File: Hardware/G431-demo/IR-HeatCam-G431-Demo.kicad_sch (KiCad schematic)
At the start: 5 parts, among them J1 Conn_SDCard, J3 Conn_UART, J4 Conn_I2C, J5 Conn_ADC1, J6 Conn_ADC2

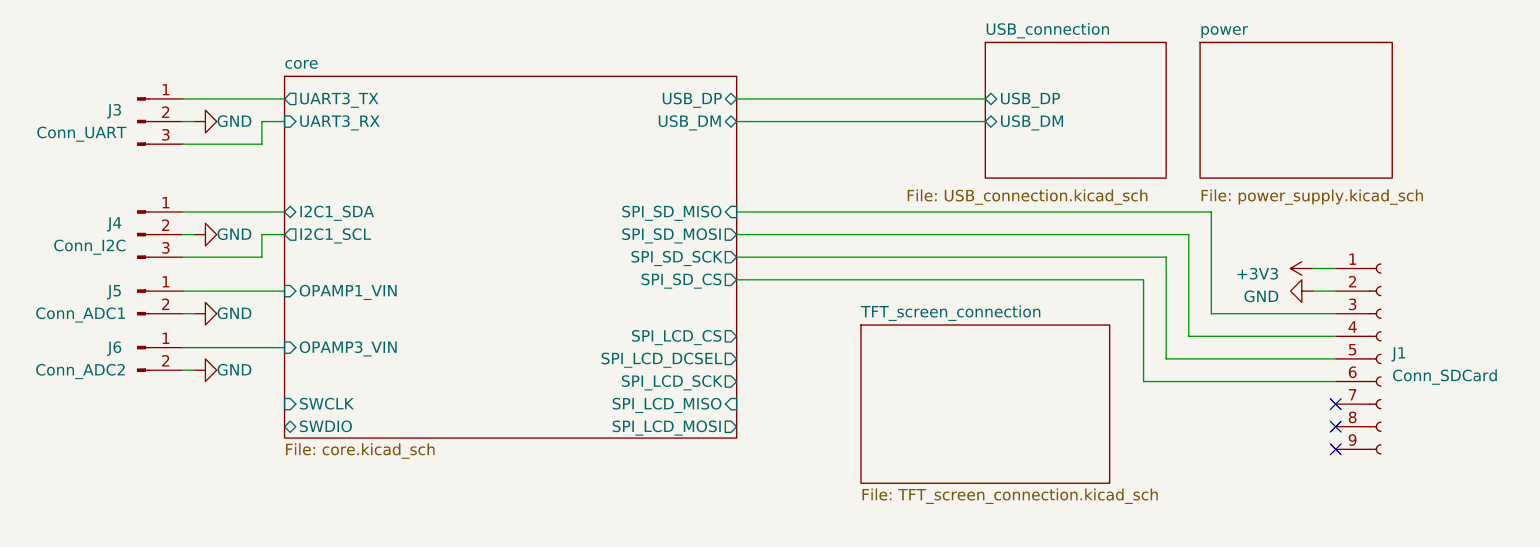
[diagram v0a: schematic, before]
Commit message: Schemetic done; PCB component layout
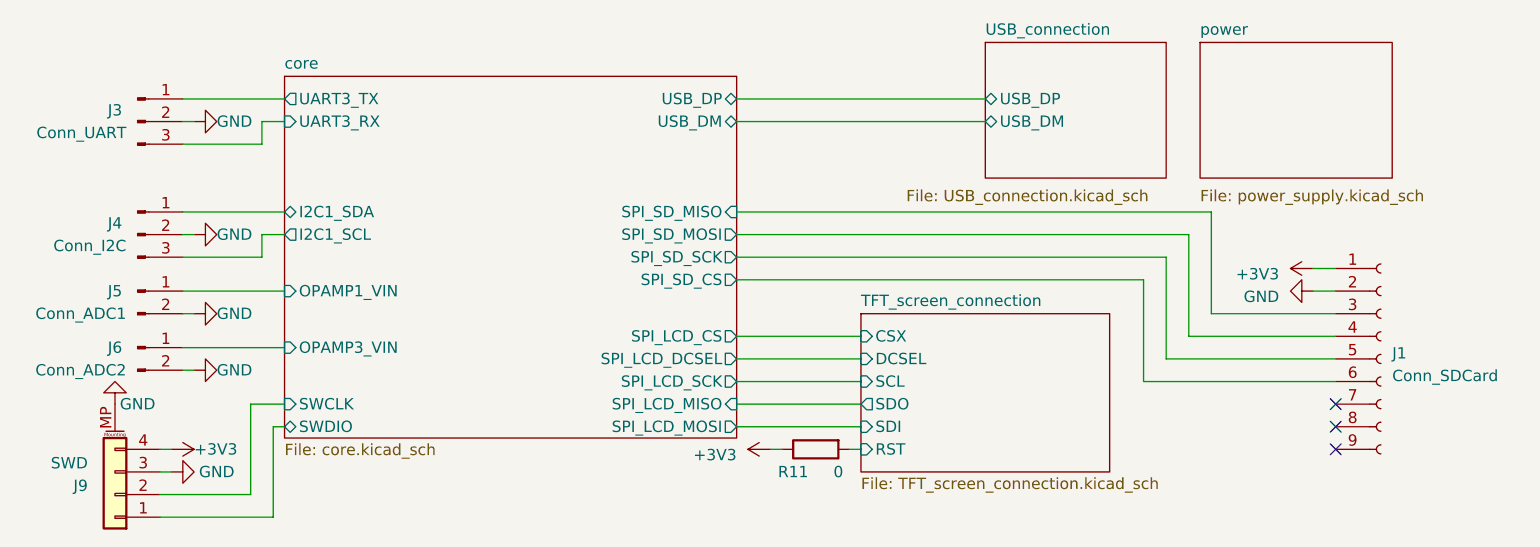
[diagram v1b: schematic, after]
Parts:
- added J9: SWD, Connector_Molex:Molex_PicoBlade_53261-0471_1x04-1MP_P1.25mm_Horizontal, symbol Connector_Generic_MountingPin:Conn_01x04_MountingPin
- added R11: 0, Resistor_SMD:R_0603_1608Metric, symbol Device:R
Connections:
- net +3V3: now also J9.4 (Pin_4), R11.1
- net GND: now also J9.3 (Pin_3), J9.MP (MountPin)
- net core/SWCLK: now also J9.2 (Pin_2)
- net core/SWDIO: now also J9.1 (Pin_1)
- new net TFT_screen_connection/RST: R11.2
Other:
- sheet TFT_screen_connection ports: added CSX, DCSEL, RST, SCL, SDI, SDO; removed none
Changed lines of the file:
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@@
+    (stroke (width 0) (type default))
+  )
+  (wire (pts (xy 87.63 124.46) (xy 87.63 134.62))
     (stroke (width 0) (type default))
   )
@@
     (stroke (width 0) (type default))
   )
+  (wire (pts (xy 88.9 124.46) (xy 87.63 124.46))
+    (stroke (width 0) (type default))
+  )
   (wire (pts (xy 86.36 105.41) (xy 77.47 105.41))
     (stroke (width 0) (type default))
   )
+  (wire (pts (xy 143.51 127) (xy 144.78 127))
+    (stroke (width 0) (type default))
+  )
   (wire (pts (xy 77.47 109.22) (xy 88.9 109.22))
     (stroke (width 0) (type default))
   )
+  (wire (pts (xy 74.93 134.62) (xy 87.63 134.62))
+    (stroke (width 0) (type default))
+  )
+  (wire (pts (xy 88.9 121.92) (xy 85.09 121.92))
+    (stroke (width 0) (type default))
+  )
+  (wire (pts (xy 139.7 124.46) (xy 153.67 124.46))
+    (stroke (width 0) (type default))
+  )
+  (wire (pts (xy 74.93 132.08) (xy 85.09 132.08))
+    (stroke (width 0) (type default))
+  )
   (wire (pts (xy 193.04 111.76) (xy 207.01 111.76))
     (stroke (width 0) (type default))
@@
     (stroke (width 0) (type default))
   )
+  (wire (pts (xy 76.2 127) (xy 74.93 127))
+    (stroke (width 0) (type default))
+  )
   (wire (pts (xy 193.04 100.33) (xy 139.7 100.33))
     (stroke (width 0) (type default))
   )
+  (wire (pts (xy 139.7 116.84) (xy 153.67 116.84))
+    (stroke (width 0) (type default))
+  )
   (wire (pts (xy 139.7 107.95) (xy 185.42 107.95))
     (stroke (width 0) (type default))
   )
+  (wire (pts (xy 74.93 129.54) (xy 76.2 129.54))
+    (stroke (width 0) (type default))
+  )
   (wire (pts (xy 204.47 106.68) (xy 207.01 106.68))
     (stroke (width 0) (type default))
@@
     (stroke (width 0) (type default))
   )
+  (wire (pts (xy 85.09 121.92) (xy 85.09 132.08))
+    (stroke (width 0) (type default))
+  )
   (wire (pts (xy 78.74 118.11) (xy 77.47 118.11))
     (stroke (width 0) (type default))
   )
+  (wire (pts (xy 139.7 114.3) (xy 153.67 114.3))
+    (stroke (width 0) (type default))
+  )
+  (wire (pts (xy 139.7 119.38) (xy 153.67 119.38))
+    (stroke (width 0) (type default))
+  )
   (wire (pts (xy 78.74 102.87) (xy 77.47 102.87))
     (stroke (width 0) (type default))
@@
     (stroke (width 0) (type default))
   )
+  (wire (pts (xy 152.4 127) (xy 153.67 127))
+    (stroke (width 0) (type default))
+  )
   (wire (pts (xy 139.7 102.87) (xy 190.5 102.87))
     (stroke (width 0) (type default))
@@
     (stroke (width 0) (type default))
   )
+  (wire (pts (xy 139.7 121.92) (xy 153.67 121.92))
+    (stroke (width 0) (type default))
+  )
   (symbol (lib_id "Connector:Conn_01x02_Pin") (at 72.39 115.57 0) (unit 1)
     (in_bom yes) (on_board yes) (dnp no)
@@
         (path "/d58afd0c-3c4a-4c6a-9275-804583496ec9"
           (reference "#PWR015") (unit 1)
+        )
+      )
+    )
+  )
+  (symbol (lib_id "power:GND") (at 69.85 121.92 180) (unit 1)
+    (in_bom yes) (on_board yes) (dnp no)
+    (property "Reference" "#PWR024" (at 69.85 115.57 0)
+      (effects (font (size 1.27 1.27)) hide)
+    )
+    (property "Value" "GND" (at 72.39 121.92 0)
+      (effects (font (size 1.27 1.27)))
+    )
+    (property "Footprint" "" (at 69.85 121.92 0)
+      (effects (font (size 1.27 1.27)) hide)
+    )
+    (property "Datasheet" "" (at 69.85 121.92 0)
+      (effects (font (size 1.27 1.27)) hide)
+    )
+    (pin "1")
+    (instances
+      (project "IR-HeatCam-G431-Demo"
+        (path "/d58afd0c-3c4a-4c6a-9275-804583496ec9"
+          (reference "#PWR024") (unit 1)
+        )
+      )
+      (project "f407_v0.4"
+        (path "/e63e39d7-6ac0-4ffd-8aa3-1841a4541b55"
+          (reference "#PWR034") (unit 1)
+        )
+      )
+    )
+  )
+  (symbol (lib_id "Connector_Generic_MountingPin:Conn_01x04_MountingPin") (at 69.85 132.08 180) (unit 1)
+    (in_bom yes) (on_board yes) (dnp no) (fields_autoplaced)
+    (property "Reference" "J9" (at 66.802 131.0894 0)
+      (effects (font (size 1.27 1.27)) (justify left))
+    )
+    (property "Value" "SWD" (at 66.802 128.5494 0)
+      (effects (font (size 1.27 1.27)) (justify left))
+    )
+    (property "Footprint" "Connector_Molex:Molex_PicoBlade_53261-0471_1x04-1MP_P1.25mm_Horizontal" (at 69.85 132.08 0)
+      (effects (font (size 1.27 1.27)) hide)
+    )
+    (property "Datasheet" "[问号]" (at 69.85 132.08 0)
+      (effects (font (size 1.27 1.27)) hide)
+    )
+    (pin "1")
+    (pin "2")
+    (pin "3")
+    (pin "4")
+    (pin "MP")
+    (instances
+      (project "IR-HeatCam-G431-Demo"
+        (path "/d58afd0c-3c4a-4c6a-9275-804583496ec9"
+          (reference "J9") (unit 1)
+        )
+      )
+      (project "f407_v0.4"
+        (path "/e63e39d7-6ac0-4ffd-8aa3-1841a4541b55"
+          (reference "J4") (unit 1)
         )
       )
@@
     )
   )
+  (symbol (lib_id "power:GND") (at 76.2 129.54 90) (mirror x) (unit 1)
+    (in_bom yes) (on_board yes) (dnp no)
+    (property "Reference" "#PWR023" (at 82.55 129.54 0)
+      (effects (font (size 1.27 1.27)) hide)
+    )
+    (property "Value" "GND" (at 81.28 129.54 90)
+      (effects (font (size 1.27 1.27)))
+    )
+    (property "Footprint" "" (at 76.2 129.54 0)
+      (effects (font (size 1.27 1.27)) hide)
+    )
+    (property "Datasheet" "" (at 76.2 129.54 0)
+      (effects (font (size 1.27 1.27)) hide)
+    )
+    (pin "1")
+    (instances
+      (project "IR-HeatCam-G431-Demo"
+        (path "/d58afd0c-3c4a-4c6a-9275-804583496ec9"
+          (reference "#PWR023") (unit 1)
+        )
+      )
+      (project "f407_v0.4"
+        (path "/e63e39d7-6ac0-4ffd-8aa3-1841a4541b55"
+          (reference "#PWR038") (unit 1)
+        )
+      )
+    )
+  )
   (symbol (lib_id "power:GND") (at 78.74 102.87 90) (unit 1)
     (in_bom yes) (on_board yes) (dnp no)
@@
     )
   )
+  (symbol (lib_id "power:+3V3") (at 76.2 127 270) (unit 1)
+    (in_bom yes) (on_board yes) (dnp no)
+    (property "Reference" "#PWR025" (at 72.39 127 0)
+      (effects (font (size 1.27 1.27)) hide)
+    )
+    (property "Value" "+3V3" (at 78.74 127 90)
+      (effects (font (size 1.27 1.27)) (justify left))
+    )
+    (property "Footprint" "" (at 76.2 127 0)
+      (effects (font (size 1.27 1.27)) hide)
+    )
+    (property "Datasheet" "" (at 76.2 127 0)
+      (effects (font (size 1.27 1.27)) hide)
+    )
+    (pin "1")
+    (instances
+      (project "IR-HeatCam-G431-Demo"
+        (path "/d58afd0c-3c4a-4c6a-9275-804583496ec9"
+          (reference "#PWR025") (unit 1)
+        )
+      )
+    )
+  )
   (symbol (lib_id "power:GND") (at 78.74 118.11 90) (unit 1)
     (in_bom yes) (on_board yes) (dnp no)
@@
     )
   )
+  (symbol (lib_id "Device:R") (at 148.59 127 90) (mirror x) (unit 1)
+    (in_bom yes) (on_board yes) (dnp no)
+    (property "Reference" "R11" (at 146.05 129.54 90)
+      (effects (font (size 1.27 1.27)))
+    )
+    (property "Value" "0" (at 151.13 129.54 90)
+      (effects (font (size 1.27 1.27)))
+    )
+    (property "Footprint" "Resistor_SMD:R_0603_1608Metric" (at 148.59 125.222 90)
+      (effects (font (size 1.27 1.27)) hide)
+    )
+    (property "Datasheet" "~" (at 148.59 127 0)
+      (effects (font (size 1.27 1.27)) hide)
+    )
+    (pin "1")
+    (pin "2")
+    (instances
+      (project "IR-HeatCam-G431-Demo"
+        (path "/d58afd0c-3c4a-4c6a-9275-804583496ec9"
+          (reference "R11") (unit 1)
+        )
+      )
+    )
+  )
   (symbol (lib_id "power:GND") (at 78.74 90.17 90) (unit 1)
     (in_bom yes) (on_board yes) (dnp no)
@@
     )
   )
-  (sheet (at 153.67 113.03) (size 27.94 17.78) (fields_autoplaced)
+  (symbol (lib_id "power:+3V3") (at 143.51 127 90) (unit 1)
+    (in_bom yes) (on_board yes) (dnp no) (fields_autoplaced)
+    (property "Reference" "#PWR022" (at 147.32 127 0)
+      (effects (font (size 1.27 1.27)) hide)
+    )
+    (property "Value" "+3V3" (at 139.7 127.635 90)
+      (effects (font (size 1.27 1.27)) (justify left))
+    )
+    (property "Footprint" "" (at 143.51 127 0)
+      (effects (font (size 1.27 1.27)) hide)
+    )
+    (property "Datasheet" "" (at 143.51 127 0)
+      (effects (font (size 1.27 1.27)) hide)
+    )
+    (pin "1")
+    (instances
+      (project "IR-HeatCam-G431-Demo"
+        (path "/d58afd0c-3c4a-4c6a-9275-804583496ec9"
+          (reference "#PWR022") (unit 1)
+        )
+      )
+    )
+  )
+  (sheet (at 153.67 111.76) (size 27.94 17.78) (fields_autoplaced)
     (stroke (width 0.1524) (type solid))
     (fill (color 0 0 0 0.0000))
-    (property "Sheetname" "TFT_screen_connection" (at 153.67 112.3184 0)
+    (property "Sheetname" "TFT_screen_connection" (at 153.67 111.0484 0)
       (effects (font (size 1.27 1.27)) (justify left bottom))
     )
-    (property "Sheetfile" "TFT_screen_connection.kicad_sch" (at 153.67 131.3946 0)
+    (property "Sheetfile" "TFT_screen_connection.kicad_sch" (at 153.67 130.1246 0)
       (effects (font (size 1.27 1.27)) (justify left top))
     )
-    (instances
+    (pin "CSX" input (at 153.67 114.3 180)
+      (effects (font (size 1.27 1.27)) (justify left))
+    )
+    (pin "SDI" input (at 153.67 124.46 180)
+      (effects (font (size 1.27 1.27)) (justify left))
+    )
+    (pin "SDO" output (at 153.67 121.92 180)
+      (effects (font (size 1.27 1.27)) (justify left))
+    )
+    (pin "SCL" input (at 153.67 119.38 180)
+      (effects (font (size 1.27 1.27)) (justify left))
+    )
+    (pin "RST" input (at 153.67 127 180)
+      (effects (font (size 1.27 1.27)) (justify left))
+    )
+    (pin "DCSEL" input (at 153.67 116.84 180)
+      (effects (font (size 1.27 1.27)) (justify left))
+    )
+    (instances

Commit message: pcb
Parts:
- J1: footprint Connector_PinSocket_2.54mm:PinSocket_1x09_P2.54mm_Vertical -> Connector_PinSocket_2.54mm:PinSocket_1x06_P2.54mm_Vertical; symbol Connector:Conn_01x09_Socket -> Connector:Conn_01x06_Pin
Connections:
- no-connect marks 3 -> 0
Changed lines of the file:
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@@
 (kicad_sch (version 20230121) (generator eeschema)
   (paper "A4")
-  (no_connect (at 207.01 124.46))
-  (no_connect (at 207.01 121.92))
-  (no_connect (at 207.01 127))
   (wire (pts (xy 185.42 119.38) (xy 185.42 107.95))
     (stroke (width 0) (type default))
@@
     )
   )
-  (symbol (lib_id "Connector:Conn_01x09_Socket") (at 212.09 116.84 0) (unit 1)
-    (in_bom yes) (on_board yes) (dnp no) (fields_autoplaced)
-    (property "Reference" "J1" (at 213.36 116.205 0)
+  (symbol (lib_id "Connector:Conn_01x06_Pin") (at 212.09 111.76 0) (mirror y) (unit 1)
+    (in_bom yes) (on_board yes) (dnp no)
+    (property "Reference" "J1" (at 214.63 110.49 0)
       (effects (font (size 1.27 1.27)) (justify left))
     )
-    (property "Value" "Conn_SDCard" (at 213.36 118.745 0)
+    (property "Value" "Conn_SDCard" (at 224.79 115.57 0)
       (effects (font (size 1.27 1.27)) (justify left))
     )
-    (property "Footprint" "Connector_PinSocket_2.54mm:PinSocket_1x09_P2.54mm_Vertical" (at 212.09 116.84 0)
-      (effects (font (size 1.27 1.27)) hide)
-    )
-    (property "Datasheet" "~" (at 212.09 116.84 0)
+    (property "Footprint" "Connector_PinSocket_2.54mm:PinSocket_1x06_P2.54mm_Vertical" (at 212.09 111.76 0)
+      (effects (font (size 1.27 1.27)) hide)
+    )
+    (property "Datasheet" "~" (at 212.09 111.76 0)
       (effects (font (size 1.27 1.27)) hide)
     )
@@
     (pin "5")
     (pin "6")
-    (pin "7")
-    (pin "8")
-    (pin "9")
-    (instances
-      (project "IR-HeatCam-G431-Demo"
+    (instances
+      (project "IR-HeatCam-G431-Demo"
